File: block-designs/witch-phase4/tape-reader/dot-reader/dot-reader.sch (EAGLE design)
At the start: 24 parts, among them U1 QRE1113, U2 QRE1113, U3 QRE1113, U4 QRE1113, U5 QRE1113, U6 QRE1113

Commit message: first cut of a functional dot-reader pcb after changes to 80mm paper
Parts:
- added C7: 10uF, resistor:C-USC0805
- added IC1, IC2, IC3, IC4, IC5, IC6: 74LVC1G14DBV, 74xx-little-us:74LVC1G14DBV
- added JP1: (no value), custom-pinhead:PINHD-1X8
- added LED1, LED2, LED3, LED4, LED5, LED6: (no value), led:LEDCHIP-LED0805
- added R13, R14, R15: 10K, resistor:R-US_M0805
- added R16, R17, R18: 270, resistor:R-US_R0805
- C1, C2, C3, C4, C5, C6: value 10nF -> 0.1uF; device resistor:C-USC0805 -> resistor:C-USC0603
- R10, R12: value 220R -> 100R
- R2: value 200R -> 100R
- R4, R6: value 220R -> 10K
- R5: value 100R -> 10K
- R7, R9: value 100R -> 270; device resistor:R-US_M0805 -> resistor:R-US_R0805
- R8: value 220R -> 270; device resistor:R-US_M0805 -> resistor:R-US_R0805
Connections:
- removed net N$12: C6.2, R12.2, U6.C
- new net !SENS_A: IC1A.I, R4.1, U1.C
- new net !SENS_B: IC2A.I, R5.1, U2.C
- new net !SENS_C: IC4A.I, R13.1, U4.C
- new net !SENS_D: IC5A.I, R14.1, U5.C
- new net !SENS_DOT: IC3A.I, R6.1, U3.C
- new net !SENS_E: IC6A.I, R15.1, U6.C
- new net N$20: LED1.A, R7.2
- net GND: now also C1.2, C2.2, C3.2, C4.2, C5.2, C6.2, C7.2, JP1.8, LED1.C, LED2.C, LED3.C, LED4.C, LED5.C, LED6.C
- net N$10: now also LED6.A, R18.2; no longer C5.2, R10.2, U5.C
- net N$11: now also R12.1; no longer R11.1
- net N$2: now also LED2.A, R8.2; no longer C1.2, R2.2, U1.C
- net N$3: now also R2.1; no longer R3.1
- net N$4: now also LED4.A, R16.2; no longer C2.2, R4.2, U2.C
- net N$5: now also R3.1; no longer R5.1
- net N$6: now also LED5.A, R17.2; no longer C3.2, R6.2, U3.C
- net N$7: now also R10.1; no longer R7.1
- net N$8: now also LED3.A, R9.2; no longer C4.2, R8.2, U4.C
- net N$9: now also R11.1; no longer R9.1
- net SENS_A: now also IC1A.O, JP1.2, R7.1; no longer R2.1
- net SENS_B: now also IC2A.O, JP1.3, R8.1; no longer R4.1
- net SENS_C: now also IC4A.O, JP1.5, R16.1; no longer R8.1
- net SENS_D: now also IC5A.O, JP1.6, R17.1; no longer R10.1
- net SENS_DOT: now also IC3A.O, JP1.4, R9.1; no longer R6.1
- net SENS_E: now also IC6A.O, JP1.7, R18.1; no longer R12.1
- net VCC: now also C7.1, JP1.1, R10.2, R12.2, R13.2, R14.2, R15.2, R2.2, R4.2, R6.2; no longer R7.2, R9.2
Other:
- moved on the sheet: C1, C2, C3, C4, C5, C6, R1, R10, R11, R12, R2, R3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

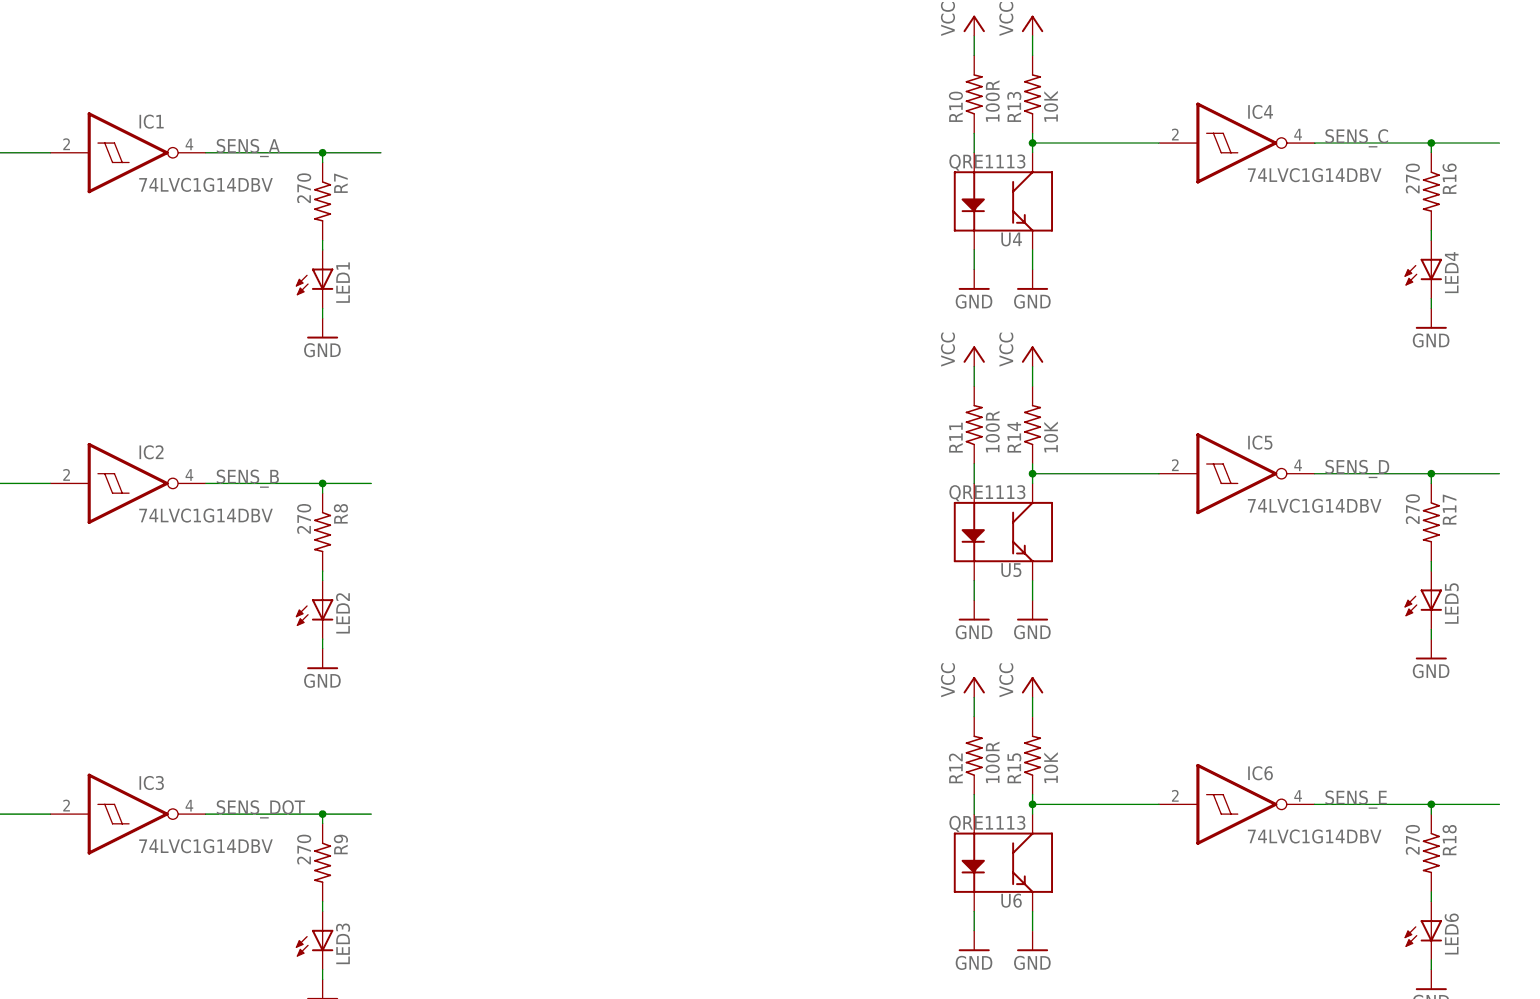
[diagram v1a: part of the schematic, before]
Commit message: switch to non-inverting schmitts and layout cleanup
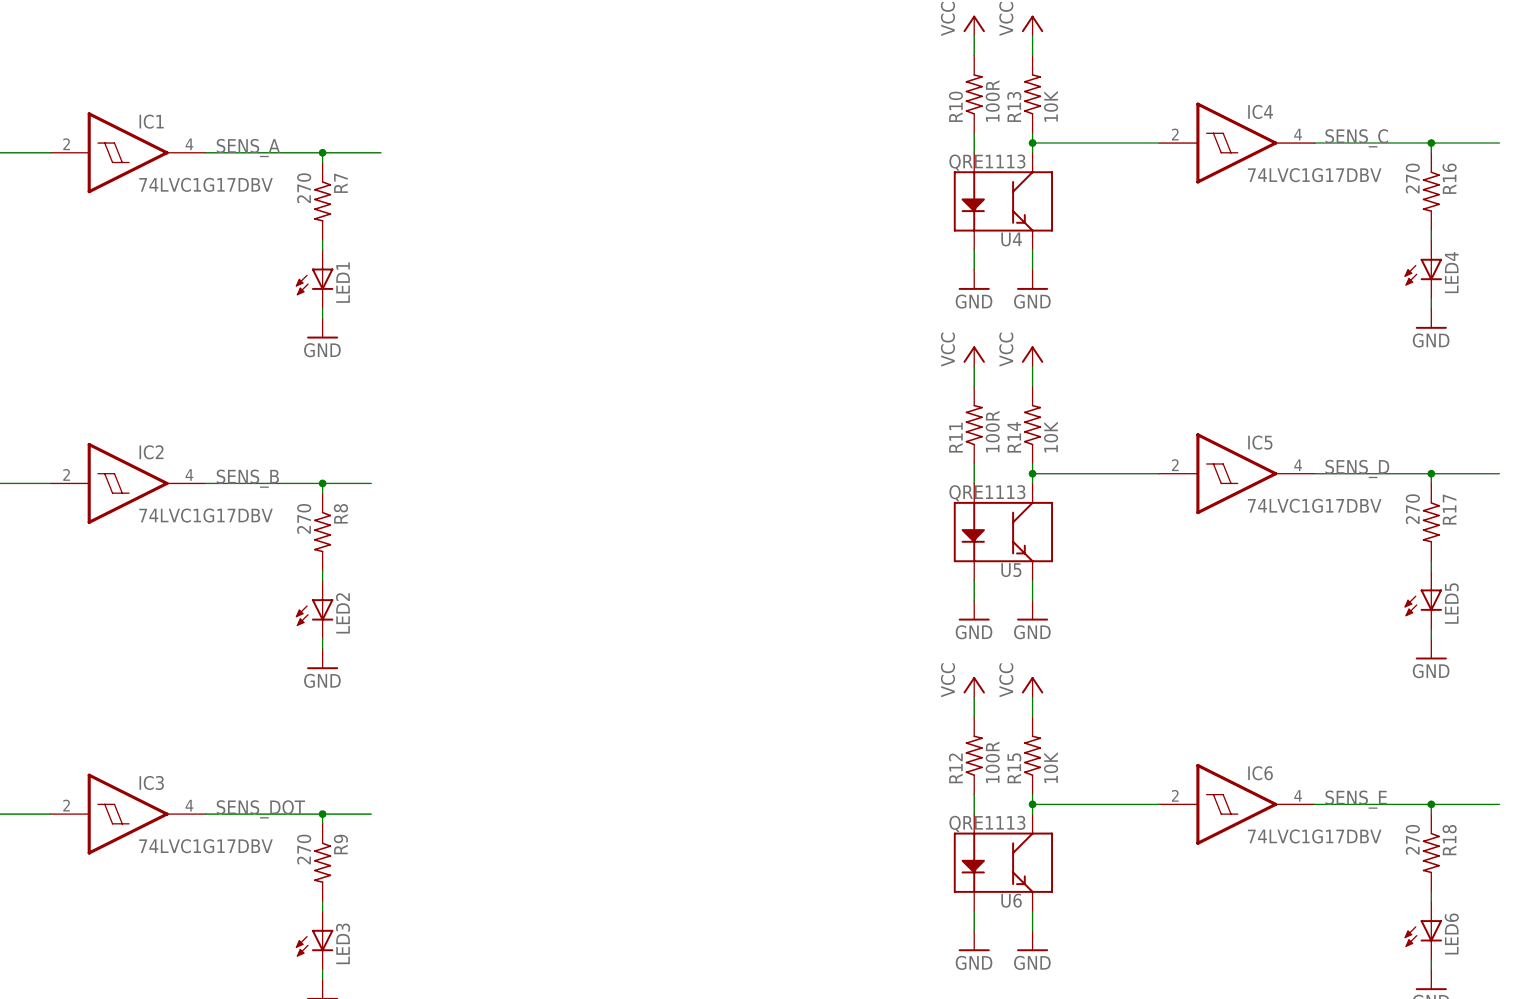
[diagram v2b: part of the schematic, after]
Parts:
- IC1, IC2, IC3, IC4, IC5, IC6: value 74LVC1G14DBV -> 74LVC1G17DBV; device 74xx-little-us:74LVC1G14DBV -> 74xx-little-us:74LVC1G17DBV
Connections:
- net !SENS_A renamed A
- net !SENS_B renamed B
- net !SENS_C renamed C
- net !SENS_D renamed D
- net !SENS_DOT renamed DOT
- net !SENS_E renamed E
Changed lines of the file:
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@@
 <part name="R6" library="resistor" deviceset="R-US_" device="M0805" value="10K"/>
 <part name="R15" library="resistor" deviceset="R-US_" device="M0805" value="10K"/>
-<part name="IC4" library="74xx-little-us" deviceset="74*1G14" device="DBV" technology="LVC"/>
-<part name="IC5" library="74xx-little-us" deviceset="74*1G14" device="DBV" technology="LVC"/>
-<part name="IC6" library="74xx-little-us" deviceset="74*1G14" device="DBV" technology="LVC"/>
-<part name="IC1" library="74xx-little-us" deviceset="74*1G14" device="DBV" technology="LVC"/>
-<part name="IC2" library="74xx-little-us" deviceset="74*1G14" device="DBV" technology="LVC"/>
-<part name="IC3" library="74xx-little-us" deviceset="74*1G14" device="DBV" technology="LVC"/>
+<part name="IC4" library="74xx-little-us" deviceset="74*1G17" device="DBV" technology="LVC"/>
+<part name="IC5" library="74xx-little-us" deviceset="74*1G17" device="DBV" technology="LVC"/>
+<part name="IC6" library="74xx-little-us" deviceset="74*1G17" device="DBV" technology="LVC"/>
+<part name="IC1" library="74xx-little-us" deviceset="74*1G17" device="DBV" technology="LVC"/>
+<part name="IC2" library="74xx-little-us" deviceset="74*1G17" device="DBV" technology="LVC"/>
+<part name="IC3" library="74xx-little-us" deviceset="74*1G17" device="DBV" technology="LVC"/>
 <part name="LED1" library="led" deviceset="LED" device="CHIP-LED0805"/>
 <part name="R7" library="resistor" deviceset="R-US_" device="R0805" value="270"/>
@@
 </segment>
 </net>
-<net name="!SENS_A" class="0">
+<net name="A" class="0">
 <segment>
 <wire x1="49.53" y1="185.42" x2="66.04" y2="185.42" width="0.1524" layer="91"/>
@@
 </segment>
 </net>
-<net name="!SENS_B" class="0">
+<net name="B" class="0">
 <segment>
 <pinref part="U2" gate="&gt;NAME" pin="C"/>
@@
 </segment>
 </net>
-<net name="!SENS_DOT" class="0">
+<net name="DOT" class="0">
 <segment>
 <pinref part="U3" gate="&gt;NAME" pin="C"/>
@@
 </segment>
 </net>
-<net name="!SENS_C" class="0">
+<net name="C" class="0">
 <segment>
 <pinref part="U4" gate="&gt;NAME" pin="C"/>
@@
 </segment>
 </net>
-<net name="!SENS_D" class="0">
+<net name="D" class="0">
 <segment>
 <pinref part="U5" gate="&gt;NAME" pin="C"/>
@@
 </segment>
 </net>
-<net name="!SENS_E" class="0">
+<net name="E" class="0">
 <segment>
 <pinref part="U6" gate="&gt;NAME" pin="C"/>

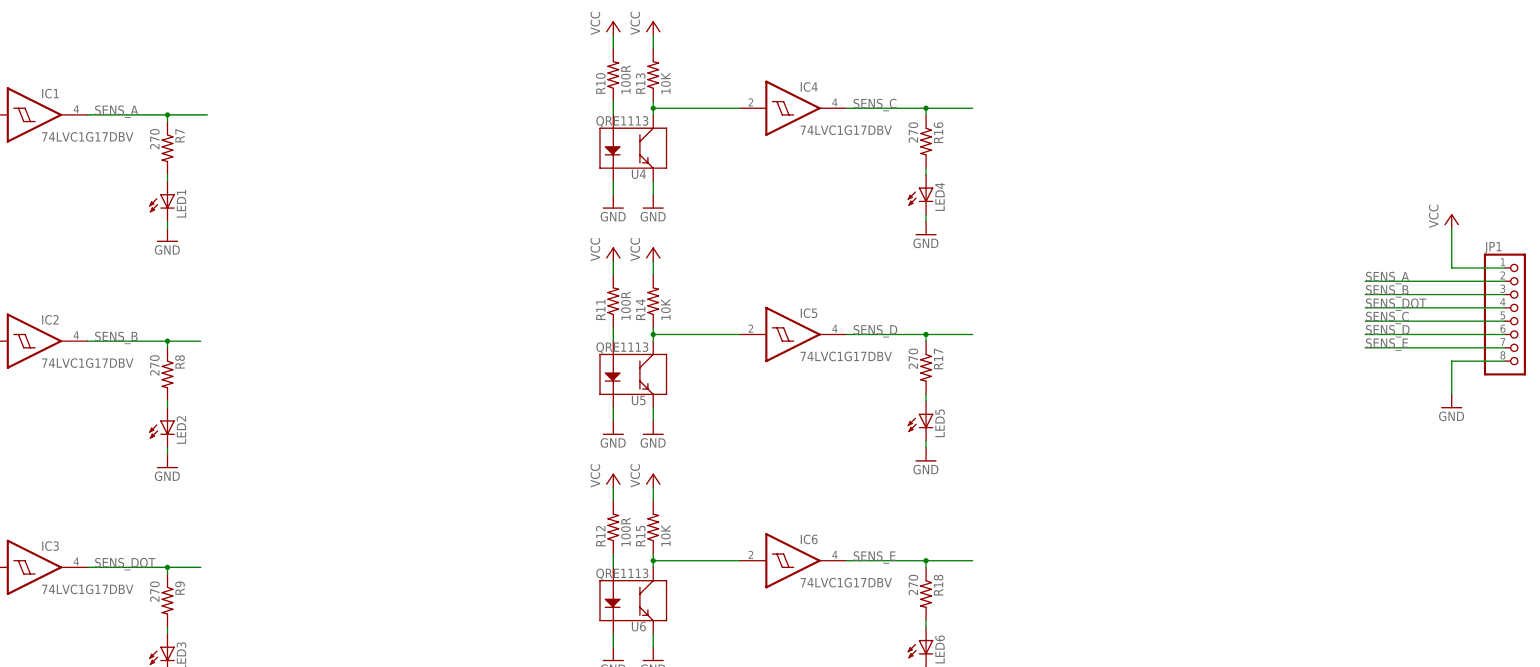
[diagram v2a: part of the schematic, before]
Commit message: fix QRE1113 pcb footprint and reverse direction of signal labels
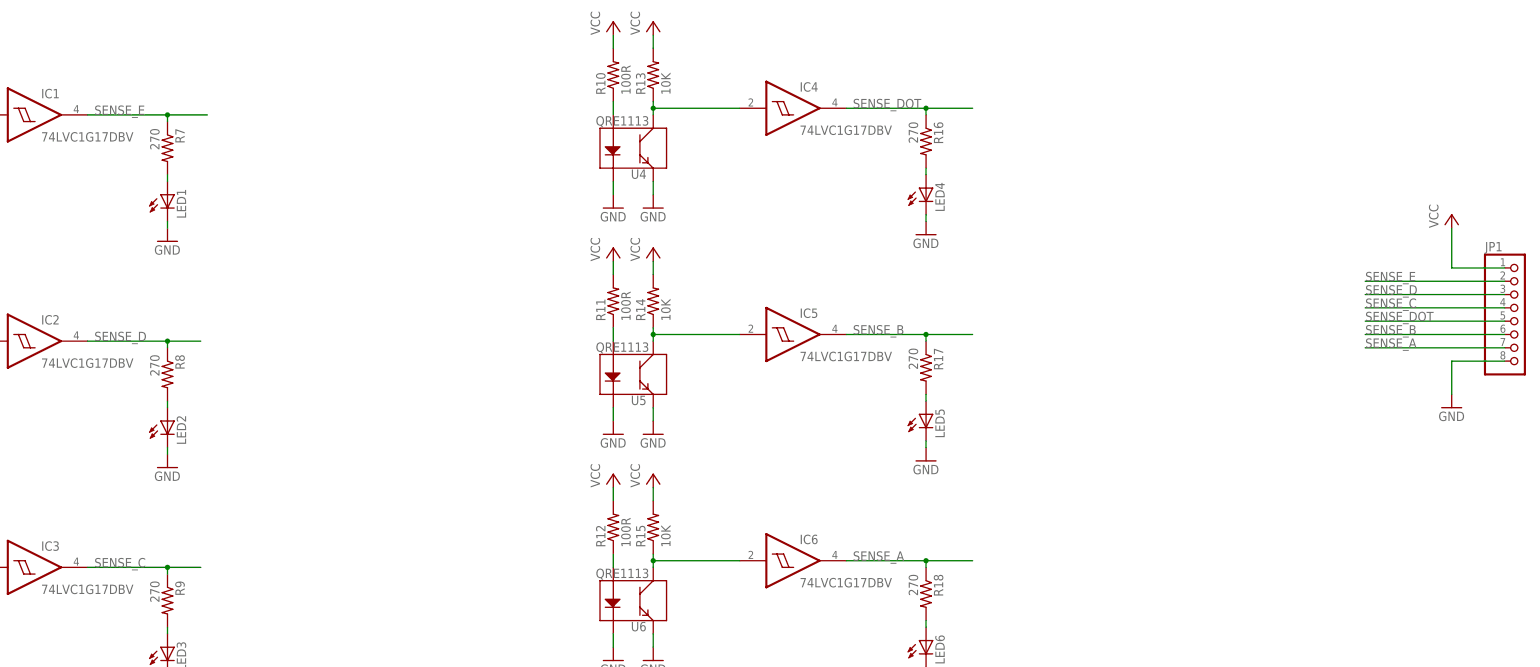
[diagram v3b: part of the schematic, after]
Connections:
- net SENS_A renamed SENSE_E
- net SENS_B renamed SENSE_D
- net SENS_C renamed SENSE_DOT
- net SENS_D renamed SENSE_B
- net SENS_DOT renamed SENSE_C
- net SENS_E renamed SENSE_A
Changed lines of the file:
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@@
 </segment>
 </net>
-<net name="SENS_E" class="0">
+<net name="SENSE_A" class="0">
 <segment>
 <pinref part="JP1" gate="A" pin="7"/>
@@
 </segment>
 </net>
-<net name="SENS_B" class="0">
+<net name="SENSE_D" class="0">
 <segment>
 <pinref part="JP1" gate="A" pin="3"/>
@@
 </segment>
 </net>
-<net name="SENS_DOT" class="0">
+<net name="SENSE_C" class="0">
 <segment>
 <pinref part="JP1" gate="A" pin="4"/>
@@
 </segment>
 </net>
-<net name="SENS_A" class="0">
+<net name="SENSE_E" class="0">
 <segment>
 <pinref part="JP1" gate="A" pin="2"/>
@@
 </segment>
 </net>
-<net name="SENS_C" class="0">
+<net name="SENSE_DOT" class="0">
 <segment>
 <pinref part="JP1" gate="A" pin="5"/>
@@
 </segment>
 </net>
-<net name="SENS_D" class="0">
+<net name="SENSE_B" class="0">
 <segment>
 <pinref part="JP1" gate="A" pin="6"/>
